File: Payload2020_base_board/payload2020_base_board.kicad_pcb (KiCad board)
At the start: 2 copper layers, 95 x 82 mm, 105 parts, among them J1 Conn_01x05, J10 Micro_SD_Card, J2 Conn_01x02, J3 Conn_01x02, J4 Conn_01x06, J5 Conn_01x08, J6 Conn_01x06, J7 Conn_01x02, J8 Conn_01x02, J9 Micro_SD_Card, Q1 Q_PMOS_GSD, Q4 Q_PMOS_GSD, Q5 Q_PMOS_GSD, SW1 SW_Push, SW2 SW_Push, U1 MCP2515-xSO, U10 MS5607-02BA, U11 SM74611, U12 SM74611, U13 CD74HC4050, U2 LD1117S33TR_SOT223, U3 CD74HC4050, U4 MCP2562-E-SN, U5 MCP2515-xSO, U6 TPS62143, U7 LT1109A, U8 MCP2562-E-SN, U9 TCA9517, Y1 16MHz, Y2 16MHz

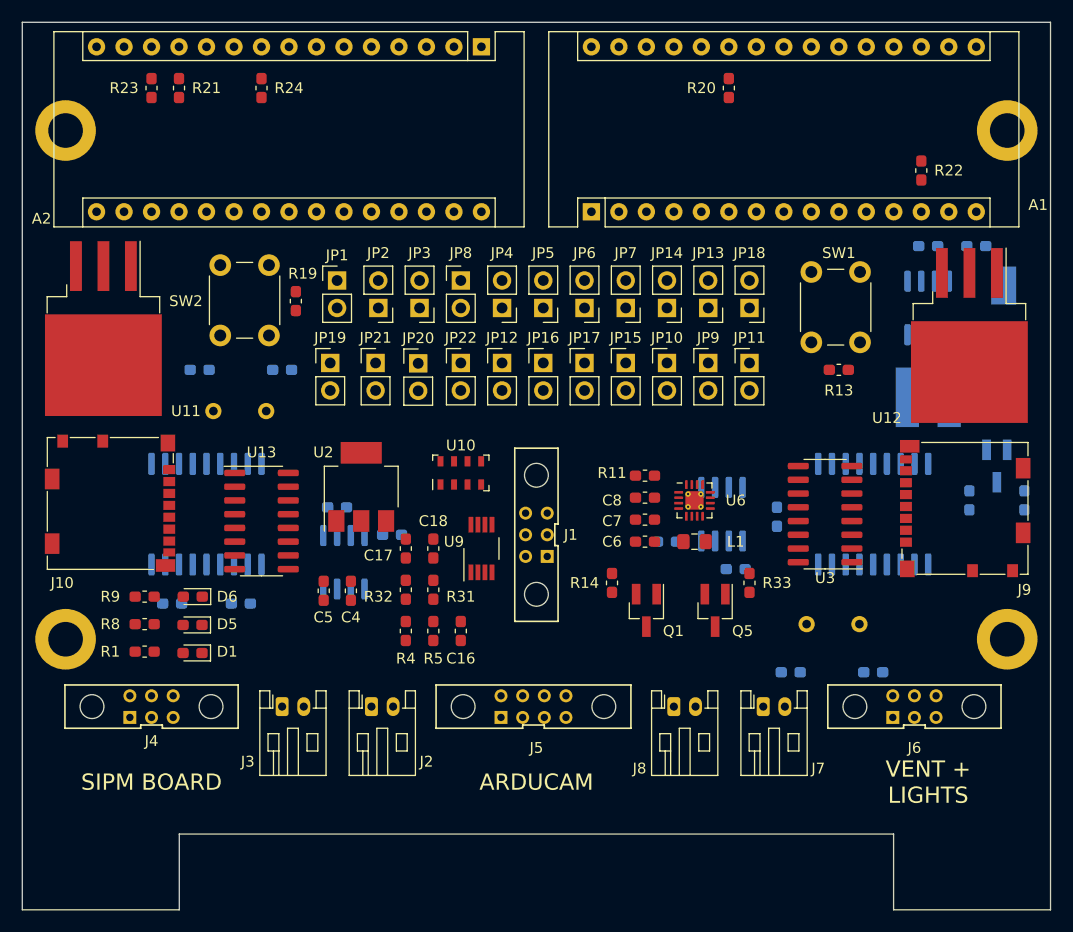
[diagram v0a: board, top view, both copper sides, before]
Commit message: added layout routing
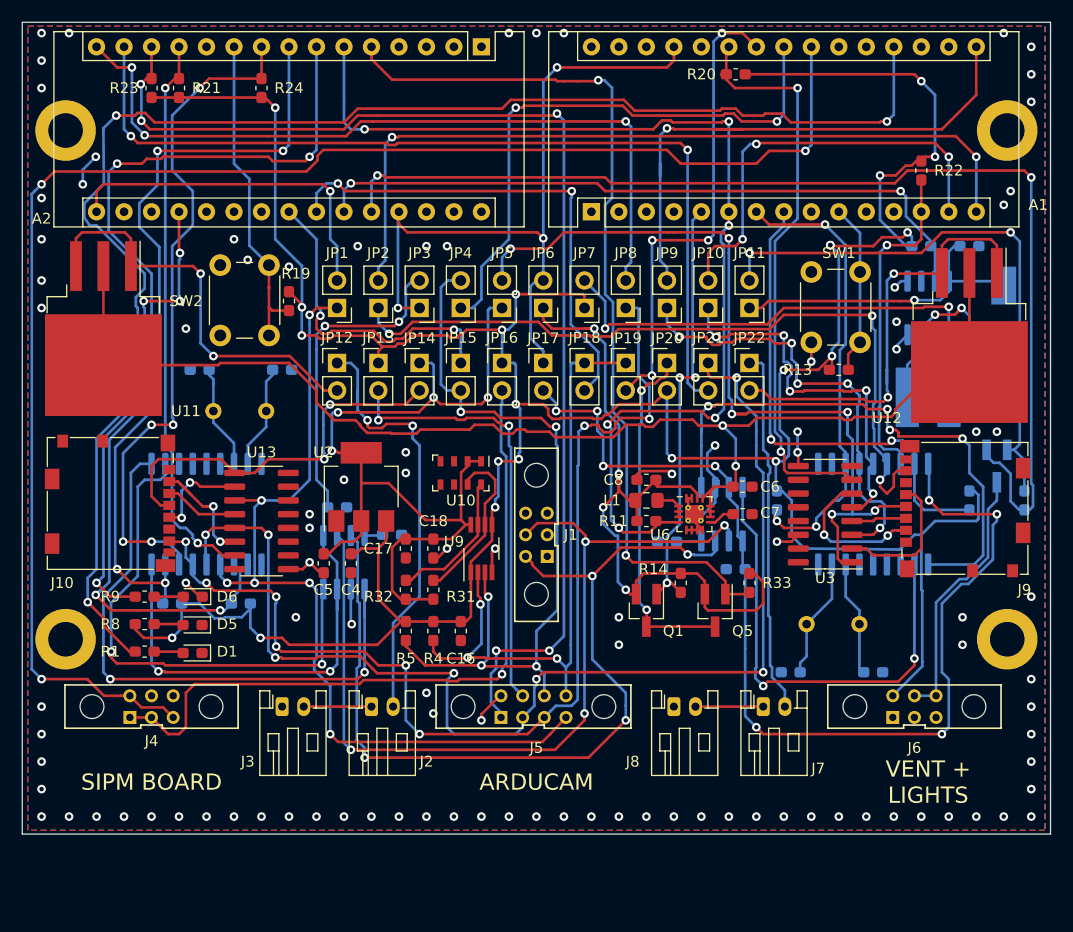
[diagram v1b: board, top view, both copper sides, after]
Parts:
- removed the JP10 at (101.0, 129.5)
- removed the JP19 at (69.8, 129.5)
- added G***: LOGO, Team_Logo:Thonk, B.Cu at (63.5, 107.3)
- added G***: LOGO, footprints:Thonk, F.Cu at (196.8, 146.1)
- added G***: LOGO, Team_Logo:Logo_Horizontal_Silkscreen_10mm, B.Cu at (110.5, 108.0)
- added JP3: Jumper, Connector_PinHeader_2.54mm:PinHeader_1x02_P2.54mm_Vertical, F.Cu at (78.1, 124.5)
- added JP8: Jumper, Connector_PinHeader_2.54mm:PinHeader_1x02_P2.54mm_Vertical, F.Cu at (97.2, 124.5)
- moved JP11 34.9 mm to (108.6, 124.5), turned to 180 degrees
- moved JP13 34.3 mm to (74.3, 129.5)
- moved JP1 27.1 mm to (70.5, 124.5), turned to 180 degrees
- moved JP22 26.7 mm to (108.6, 129.5)
- moved JP14 23.4 mm to (78.1, 129.5), turned to 0 degrees
- moved JP17 19.7 mm to (89.5, 129.5), turned to 0 degrees
- moved JP19 19.7 mm to (97.2, 129.5), turned to 0 degrees
- moved JP10 19.1 mm to (104.8, 124.5)
- moved JP5 19.1 mm to (85.7, 124.5)
- moved JP7 16.2 mm to (93.3, 124.5), turned to 180 degrees
- moved JP2 15.2 mm to (74.3, 124.5)
- moved JP6 15.2 mm to (89.5, 124.5)
- moved C6 10.3 mm to (108.0, 141.0), turned to 0 degrees
- moved C7 9.03 mm to (108.0, 143.5), turned to 0 degrees
- moved JP9 7.62 mm to (101.0, 124.5)
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- renumbered JP15 to JP1, JP4 to JP10, JP21 to JP11, JP1 to JP12, JP11 to JP13, JP16 to JP15, JP12 to JP16, JP18 to JP17, JP17 to JP18, JP3 to JP19, JP5 to JP2, JP7 to JP20, JP9 to JP21, JP8 to JP4, JP13 to JP5, JP2 to JP6, JP20 to JP7, JP6 to JP9
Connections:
- A1 pad 19: (no net) -> /LED1
- R1 pad 1: /LED2 -> /LED1
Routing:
- net +5V: track 0.00 -> 305.1 mm, vias 0 -> 21
- net Net-(A1-Pad22): track 0.00 -> 143.1 mm, vias 0 -> 3
- net /LED1: track 0.00 -> 138.7 mm, vias 0 -> 3
- net /battery_management/VIN: track 0.00 -> 119.8 mm, vias 0 -> 2
- net /SS4: track 0.00 -> 109.1 mm, vias 0 -> 5
- net /MOSI2: track 0.00 -> 109.0 mm, vias 0 -> 7
- net /~VALVE_EN: track 0.00 -> 104.1 mm, vias 0 -> 2
- net /CAN HW/CAN_5v: track 0.00 -> 99.1 mm, vias 0 -> 8
- net /MISO2: track 0.00 -> 98.7 mm, vias 0 -> 8
- net /PG: track 0.00 -> 98.6 mm, vias 0 -> 6
- net /~CAN_INT_2: track 0.00 -> 91.2 mm, vias 0 -> 4
- net Net-(A2-Pad14): track 0.00 -> 84.3 mm, vias 0 -> 2
- net +3V3: track 0.00 -> 83.0 mm, vias 0 -> 4
- net /PWR_EN2: track 0.00 -> 82.5 mm, vias 0 -> 2
- net /CAN HW/CANH: track 0.00 -> 82.3 mm, vias 0 -> 4
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- added copper zone on B.Cu, net GND
- added copper zone on F.Cu, net GND
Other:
- board size 95 x 82 mm -> 95 x 75 mm
- board text added: "R1"
- board text added: "THONK"

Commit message: updated schematic based on aarons PR comments
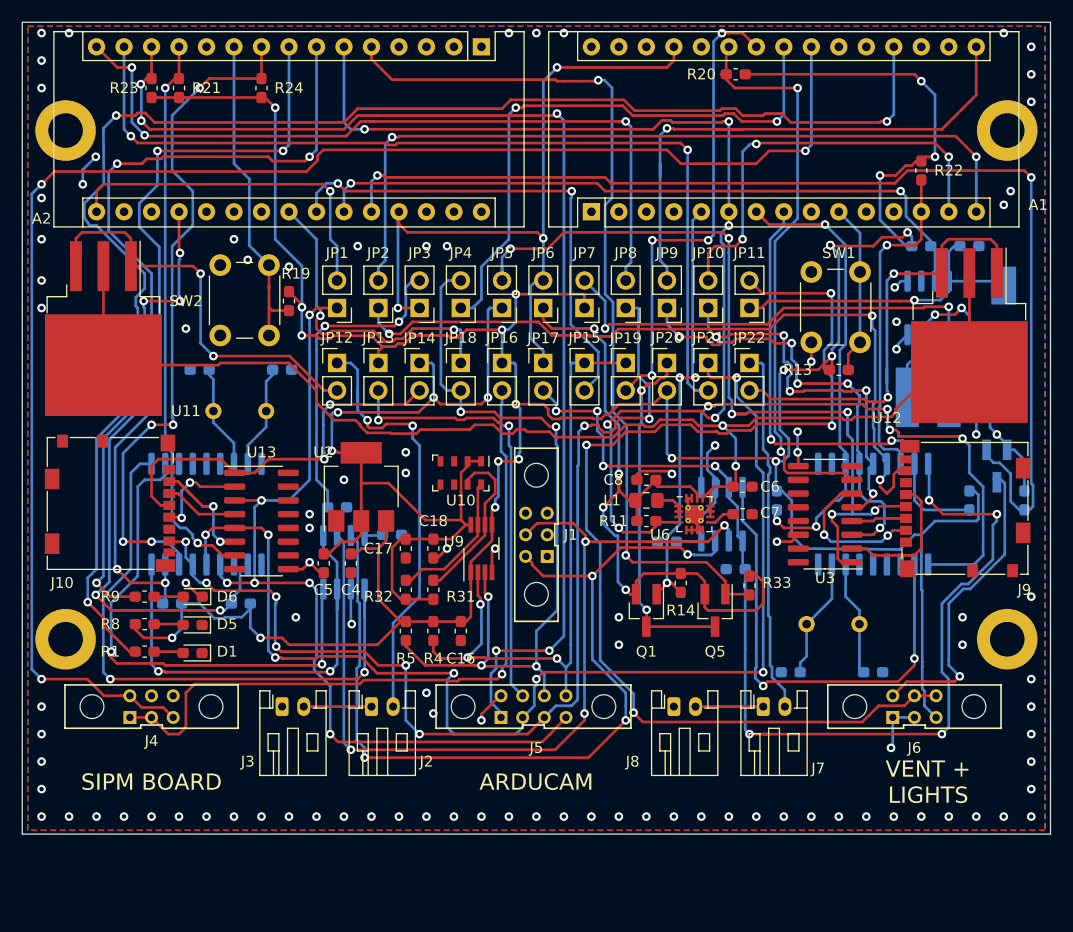
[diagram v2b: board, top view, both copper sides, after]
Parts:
- Q4: value Q_PMOS_GSD -> Q_NMOS_GSD
- moved R33 0.24 mm to (108.6, 150.1)
- turned R1 to 180 degrees
- turned R16 to 90 degrees
- turned R9 to 180 degrees
- renumbered JP18 to JP15, JP15 to JP18
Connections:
- net /battery_management/VOUT renamed Net-(C8-Pad1)
- net /~CAN_INT_1 renamed /CAN HW/~INT
- net /~CAN_INT_2 renamed /sheet5E2B166E/~INT
- net /~CAN_RESET_1 renamed /CAN HW/~RESET
- net /~CAN_RESET_2 renamed /sheet5E2B166E/~RESET
- net /~VALVE_SHUTDOWN renamed /Valve Controller/~SHUTDOWN
- A1 pad 1: (no net) -> Net-(A1-Pad1)
- A1 pad 11: (no net) -> Net-(A1-Pad11)
- A1 pad 12: (no net) -> Net-(A1-Pad12)
- A1 pad 17: (no net) -> Net-(A1-Pad17)
- A1 pad 18: (no net) -> Net-(A1-Pad18)
- A1 pad 19: /LED1 -> Net-(A1-Pad19)
- A1 pad 2: (no net) -> Net-(A1-Pad2)
- A1 pad 20: (no net) -> Net-(A1-Pad20)
- A1 pad 21: (no net) -> Net-(A1-Pad21)
- A1 pad 26: (no net) -> Net-(A1-Pad26)
- A1 pad 28: (no net) -> Net-(A1-Pad28)
- A1 pad 3: (no net) -> Net-(A1-Pad3)
- A1 pad 30: (no net) -> Net-(A1-Pad30)
- A1 pad 9: (no net) -> Net-(A1-Pad9)
- A2 pad 1: (no net) -> Net-(A2-Pad1)
- A2 pad 11: (no net) -> Net-(A2-Pad11)
- A2 pad 17: (no net) -> Net-(A2-Pad17)
- A2 pad 18: (no net) -> Net-(A2-Pad18)
- A2 pad 19: /LED2 -> Net-(A2-Pad19)
- A2 pad 2: (no net) -> Net-(A2-Pad2)
- A2 pad 20: (no net) -> Net-(A2-Pad20)
- A2 pad 21: (no net) -> Net-(A2-Pad21)
- A2 pad 22: (no net) -> Net-(A2-Pad22)
- A2 pad 26: /~VALVE_EN -> /Valve Controller/VALVE_EN
- A2 pad 28: (no net) -> Net-(A2-Pad28)
- A2 pad 3: (no net) -> Net-(A2-Pad3)
- A2 pad 30: (no net) -> Net-(A2-Pad30)
- J1 pad 1: (no net) -> Net-(J1-Pad1)
- J1 pad 2: (no net) -> Net-(J1-Pad2)
- J10 pad 1: (no net) -> Net-(J10-Pad1)
- J10 pad 8: (no net) -> Net-(J10-Pad8)
- J6 pad 3: GND -> +5V
- J6 pad 4: +5V -> /Valve Controller/VALVE-
- J9 pad 1: (no net) -> Net-(J9-Pad1)
- J9 pad 8: (no net) -> Net-(J9-Pad8)
- JP11 pad 2: Net-(JP11-Pad2) -> /Valve Controller/VALVE+
- Q4 pad 1: /~VALVE_EN -> /Valve Controller/VALVE_EN
- Q4 pad 2: Net-(JP11-Pad2) -> GND
- Q4 pad 3: /Valve Controller/VALVE+ -> /Valve Controller/VALVE-
- R1 pad 1: /LED1 -> Net-(D1-Pad2)
- R1 pad 2: Net-(D1-Pad2) -> Net-(A1-Pad19)
- R16 pad 1: Net-(JP11-Pad2) -> /Valve Controller/VALVE_EN
- R16 pad 2: /~VALVE_EN -> GND
- R9 pad 1: /LED2 -> Net-(D6-Pad2)
- R9 pad 2: Net-(D6-Pad2) -> Net-(A2-Pad19)
- U1 pad 10: (no net) -> Net-(U1-Pad10)
- U1 pad 11: (no net) -> Net-(U1-Pad11)
- U1 pad 3: (no net) -> Net-(U1-Pad3)
- U1 pad 4: (no net) -> Net-(U1-Pad4)
- U1 pad 5: (no net) -> Net-(U1-Pad5)
- U1 pad 6: (no net) -> Net-(U1-Pad6)
- U10 pad 6: (no net) -> Net-(U10-Pad6)
- U13 pad 10: (no net) -> Net-(U13-Pad10)
- U13 pad 12: (no net) -> Net-(U13-Pad12)
- U13 pad 13: (no net) -> Net-(U13-Pad13)
- U13 pad 15: (no net) -> Net-(U13-Pad15)
- U13 pad 16: (no net) -> Net-(U13-Pad16)
- U3 pad 10: (no net) -> Net-(U3-Pad10)
- U3 pad 12: (no net) -> Net-(U3-Pad12)
- U3 pad 13: (no net) -> Net-(U3-Pad13)
- U3 pad 15: (no net) -> Net-(U3-Pad15)
- U3 pad 16: (no net) -> Net-(U3-Pad16)
- U5 pad 10: (no net) -> Net-(U5-Pad10)
- U5 pad 11: (no net) -> Net-(U5-Pad11)
- U5 pad 3: (no net) -> Net-(U5-Pad3)
- U5 pad 4: (no net) -> Net-(U5-Pad4)
- U5 pad 5: (no net) -> Net-(U5-Pad5)
- U5 pad 6: (no net) -> Net-(U5-Pad6)
- U7 pad 2: (no net) -> Net-(U7-Pad2)
- U7 pad 6: (no net) -> Net-(U7-Pad6)
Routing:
- net Net-(A1-Pad19): track 0.00 -> 138.7 mm, vias 0 -> 3
- net /LED1: track 138.7 -> 0.00 mm, vias 3 -> 0
- net /~VALVE_EN: track 104.1 -> 0.00 mm, vias 2 -> 0
- net /Valve Controller/VALVE_EN: track 0.00 -> 104.1 mm, vias 0 -> 2
- net /Valve Controller/VALVE+: track 24.4 -> 101.0 mm, vias 0 -> 4
- net Net-(JP11-Pad2): track 52.9 -> 0.00 mm, vias 2 -> 0
- net Net-(A2-Pad19): track 0.00 -> 43.7 mm, vias 0 -> 4
- net /LED2: track 43.7 -> 0.00 mm, vias 4 -> 0
- net /Valve Controller/VALVE-: track 0.00 -> 29.4 mm, vias 0 -> 1
- net GND: track 47.0 -> 64.7 mm, vias 98 -> 99
- net +5V: track 305.1 -> 306.5 mm
- net /CAN HW/CAN_5v: track 99.1 -> 100.5 mm
